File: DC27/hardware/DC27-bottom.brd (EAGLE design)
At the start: 102.4 x 117.6 mm, 95 parts, among them IC2 LDL112D33R, IC3 FT2232HL-REEL, IC4 93LC46BT-I_OT, J1 PAIRING, J2 JTAG, J3 Battery, J4 Program Port, U2 ESP-WROOM-32, Y1 ABM7-12.000MHZ-D2Y-T

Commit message: moved vias
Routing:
- net PROG_TX: track 63.8 -> 66.4 mm
- net PAIR_RX: track 133.3 -> 134.6 mm
- net PAIR_TX: track 132.0 -> 131.4 mm

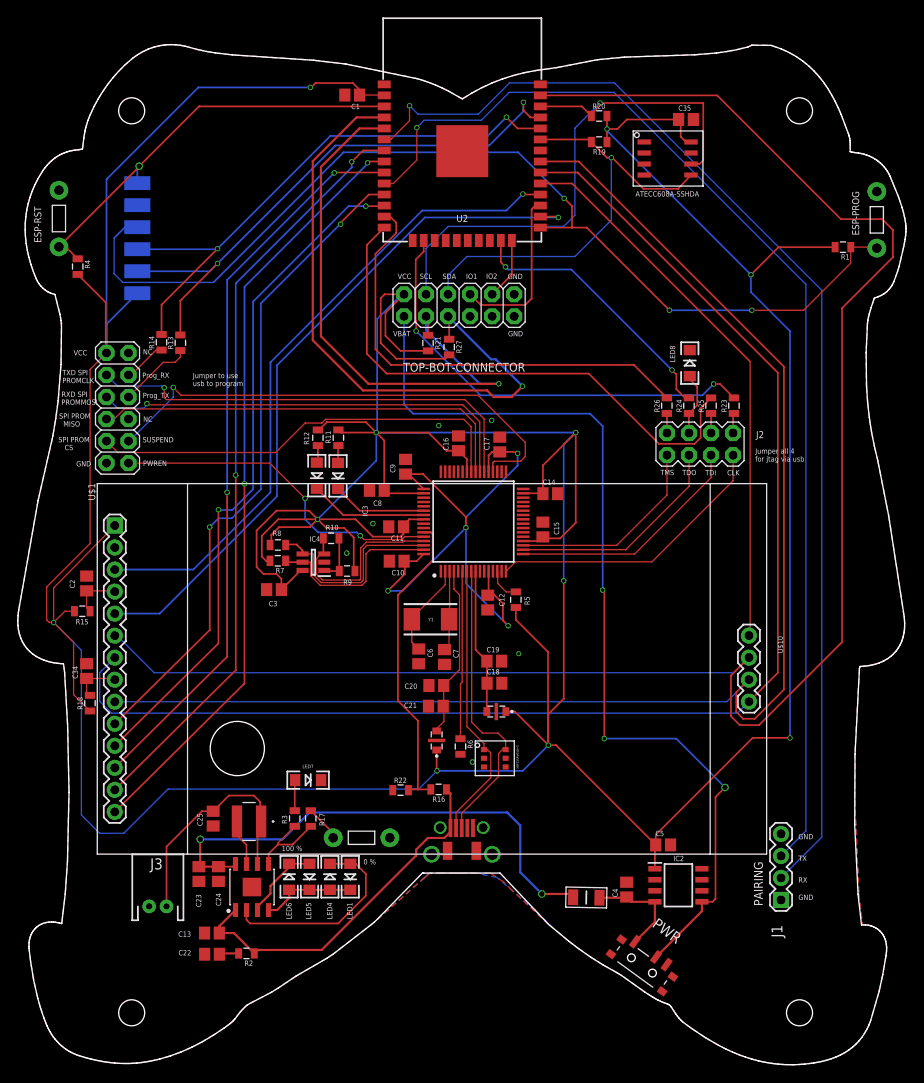
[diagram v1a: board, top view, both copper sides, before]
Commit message: Fixed the darknet logo, and made resistors pretty
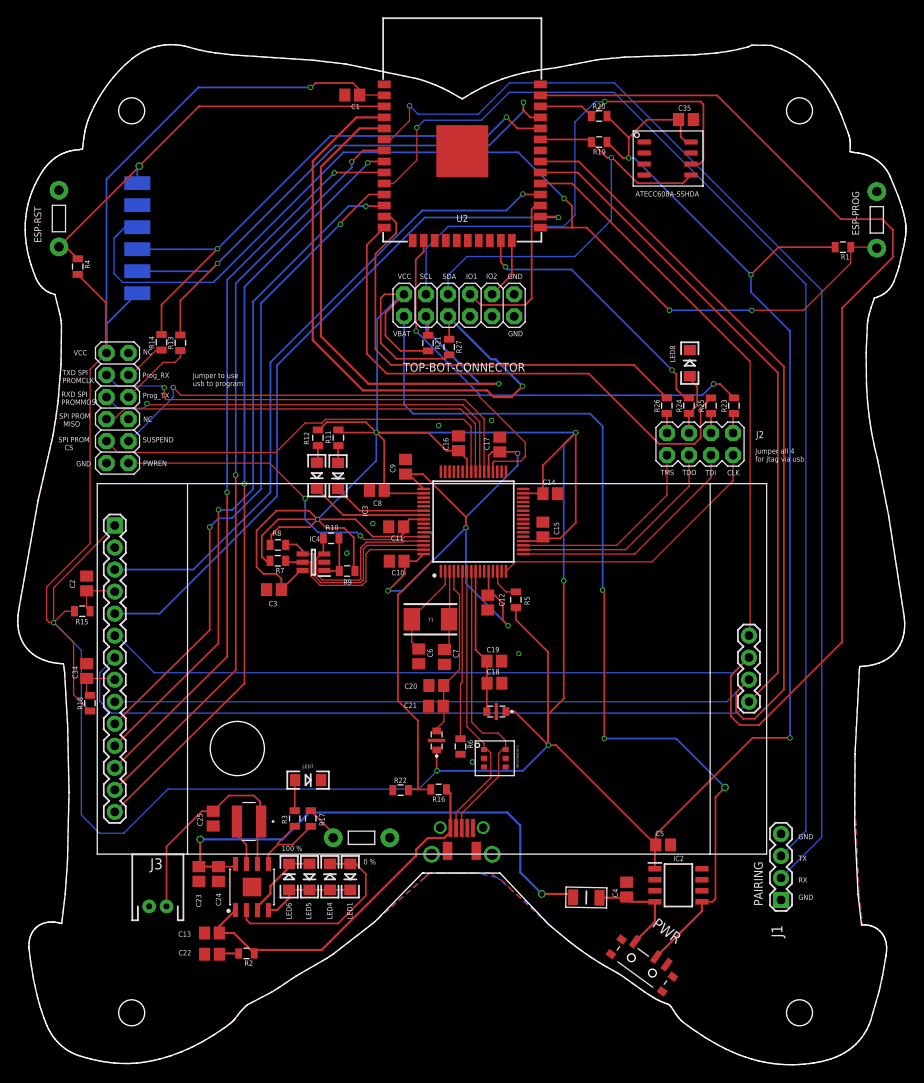
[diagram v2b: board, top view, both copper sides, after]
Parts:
- U$9: value DN_LOGO -> DN_LOGODC26; device logos:DN_LOGO_LONG_SILK -> darknet_parts_library:DN_LOGO_DC26
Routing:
- net SCL: track 66.4 -> 67.4 mm
- net SDA: track 51.3 -> 50.7 mm

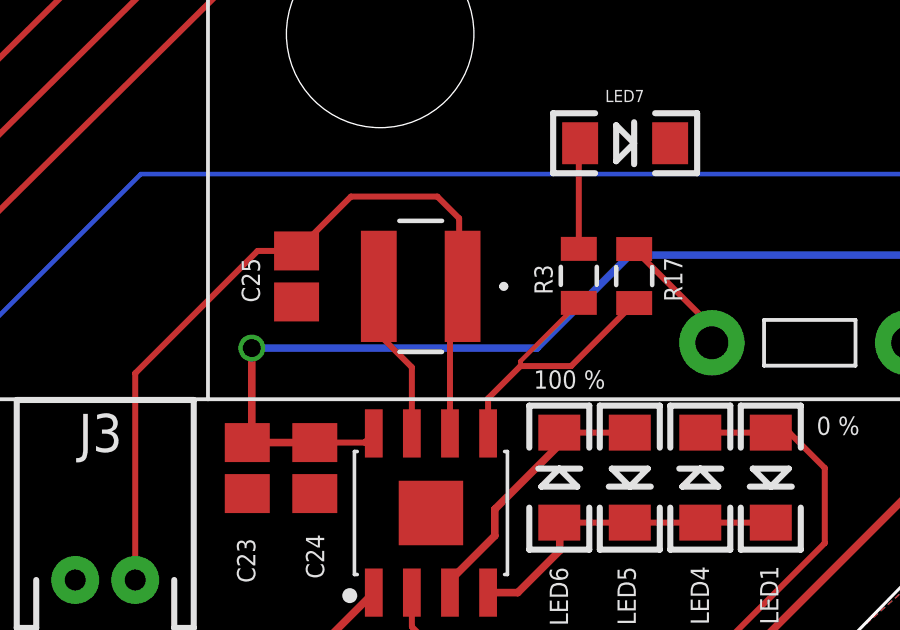
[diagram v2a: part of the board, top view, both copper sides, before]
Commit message: fixed an airwire, changed diodes to through hole
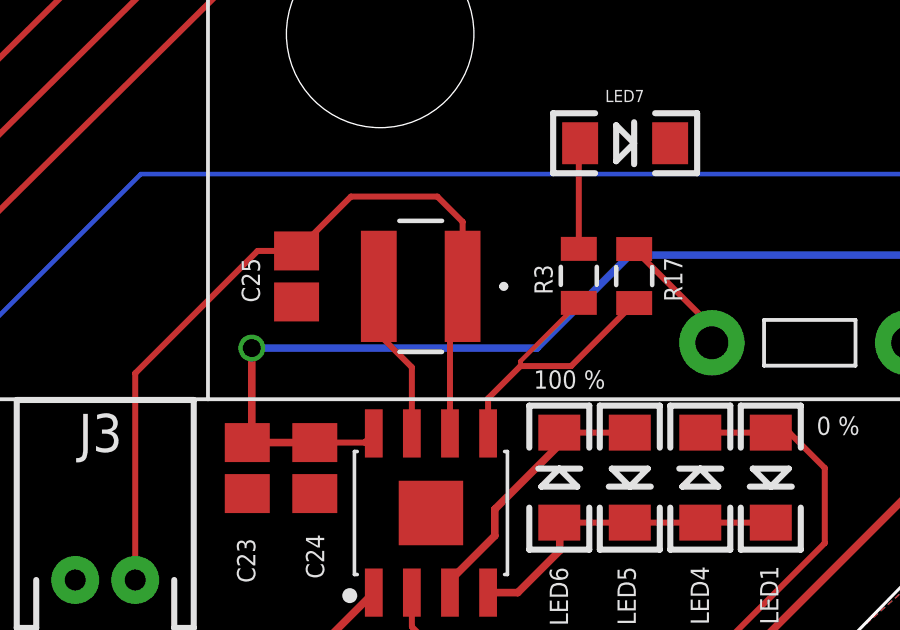
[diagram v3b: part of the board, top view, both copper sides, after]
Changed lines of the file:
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@@
 <?xml version="1.0" encoding="utf-8"?>
 <!DOCTYPE eagle SYSTEM "eagle.dtd">
-<eagle version="9.4.0">
+<eagle version="9.4.1">
 <drawing>
 <settings>
-<setting alwaysvectorfont="no"/>
+<setting alwaysvectorfont="yes"/>
 <setting keepoldvectorfont="yes"/>
 <setting verticaltext="up"/>
@@
 <layer number="14" name="Route14" color="22" fill="1" visible="no" active="no"/>
 <layer number="15" name="Route15" color="23" fill="1" visible="no" active="no"/>
-<layer number="16" name="Bottom" color="1" fill="1" visible="no" active="yes"/>
+<layer number="16" name="Bottom" color="1" fill="1" visible="yes" active="yes"/>
 <layer number="17" name="Pads" color="2" fill="1" visible="yes" active="yes"/>
 <layer number="18" name="Vias" color="2" fill="1" visible="yes" active="yes"/>
@@
 <layer number="20" name="Dimension" color="24" fill="1" visible="yes" active="yes"/>
 <layer number="21" name="tPlace" color="7" fill="1" visible="yes" active="yes"/>
-<layer number="22" name="bPlace" color="7" fill="1" visible="no" active="yes"/>
+<layer number="22" name="bPlace" color="7" fill="1" visible="yes" active="yes"/>
 <layer number="23" name="tOrigins" color="15" fill="1" visible="yes" active="yes"/>
-<layer number="24" name="bOrigins" color="15" fill="1" visible="no" active="yes"/>
+<layer number="24" name="bOrigins" color="15" fill="1" visible="yes" active="yes"/>
 <layer number="25" name="tNames" color="7" fill="1" visible="yes" active="yes"/>
-<layer number="26" name="bNames" color="7" fill="1" visible="no" active="yes"/>
+<layer number="26" name="bNames" color="7" fill="1" visible="yes" active="yes"/>
 <layer number="27" name="tValues" color="7" fill="1" visible="no" active="yes"/>
 <layer number="28" name="bValues" color="7" fill="1" visible="no" active="yes"/>
@@
 <layer number="38" name="bTest" color="7" fill="1" visible="no" active="yes"/>
 <layer number="39" name="tKeepout" color="4" fill="11" visible="yes" active="yes"/>
-<layer number="40" name="bKeepout" color="1" fill="11" visible="no" active="yes"/>
+<layer number="40" name="bKeepout" color="1" fill="11" visible="yes" active="yes"/>
 <layer number="41" name="tRestrict" color="4" fill="10" visible="yes" active="yes"/>
-<layer number="42" name="bRestrict" color="1" fill="10" visible="no" active="yes"/>
+<layer number="42" name="bRestrict" color="1" fill="10" visible="yes" active="yes"/>
 <layer number="43" name="vRestrict" color="2" fill="10" visible="no" active="yes"/>
 <layer number="44" name="Drills" color="7" fill="1" visible="no" active="yes"/>
-<layer number="45" name="Holes" color="7" fill="1" visible="yes" active="yes"/>
+<layer number="45" name="Holes" color="7" fill="1" visible="no" active="yes"/>
 <layer number="46" name="Milling" color="3" fill="1" visible="no" active="yes"/>
 <layer number="47" name="Measures" color="7" fill="1" visible="no" active="yes"/>
@@
 <layer number="50" name="dxf" color="7" fill="1" visible="no" active="no"/>
 <layer number="51" name="tDocu" color="7" fill="1" visible="yes" active="yes"/>
-<layer number="52" name="bDocu" color="7" fill="1" visible="no" active="yes"/>
+<layer number="52" name="bDocu" color="7" fill="1" visible="yes" active="yes"/>
 <layer number="53" name="tGND_GNDA" color="7" fill="9" visible="no" active="no"/>
 <layer number="54" name="bGND_GNDA" color="1" fill="9" visible="no" active="no"/>
@@
 <contactref element="C25" pad="1"/>
 <contactref element="J3" pad="2"/>
-<wire x1="28.061628125" y1="28.045459375" x2="28.061628125" y2="28.2" width="0.2" layer="1"/>
 <wire x1="22.526540625" y1="29.226628125" x2="21.226628125" y2="29.226628125" width="0.2" layer="1"/>
 <wire x1="17.149028125" y1="25.149028125" x2="17.149028125" y2="18.258659375" width="0.2" layer="1"/>
 <wire x1="21.226628125" y1="29.226628125" x2="17.149028125" y2="25.149028125" width="0.2" layer="1"/>
-<wire x1="27.640428125" y1="27.7788" x2="28.061628125" y2="28.2" width="0.2" layer="1"/>
-<wire x1="27.640428125" y1="23.144359375" x2="27.640428125" y2="27.7788" width="0.2" layer="1"/>
 <wire x1="24.33815625" y1="31.03824375" x2="27.22058125" y2="31.03824375" width="0.2" layer="1"/>
 <wire x1="24.33815625" y1="31.03824375" x2="22.526540625" y2="29.226628125" width="0.2" layer="1"/>
-<wire x1="27.22058125" y1="31.03824375" x2="27.9457375" y2="30.3130875" width="0.2" layer="1"/>
-<wire x1="27.9457375" y1="30.3130875" x2="27.9457375" y2="28.7218875" width="0.2" layer="1"/>
-<wire x1="27.9457375" y1="28.7218875" x2="28.061628125" y2="28.2" width="0" layer="19" extent="1-1"/>
+<wire x1="27.640428125" y1="23.144359375" x2="27.640428125" y2="27.624259375" width="0.2" layer="1"/>
+<wire x1="27.640428125" y1="27.624259375" x2="28.061628125" y2="28.045459375" width="0.2" layer="1"/>
+<wire x1="27.22058125" y1="31.03824375" x2="28.061628125" y2="30.197196875" width="0.2" layer="1"/>
+<wire x1="28.061628125" y1="30.197196875" x2="28.061628125" y2="28.045459375" width="0.2" layer="1"/>
 </signal>
 <signal name="N$21">

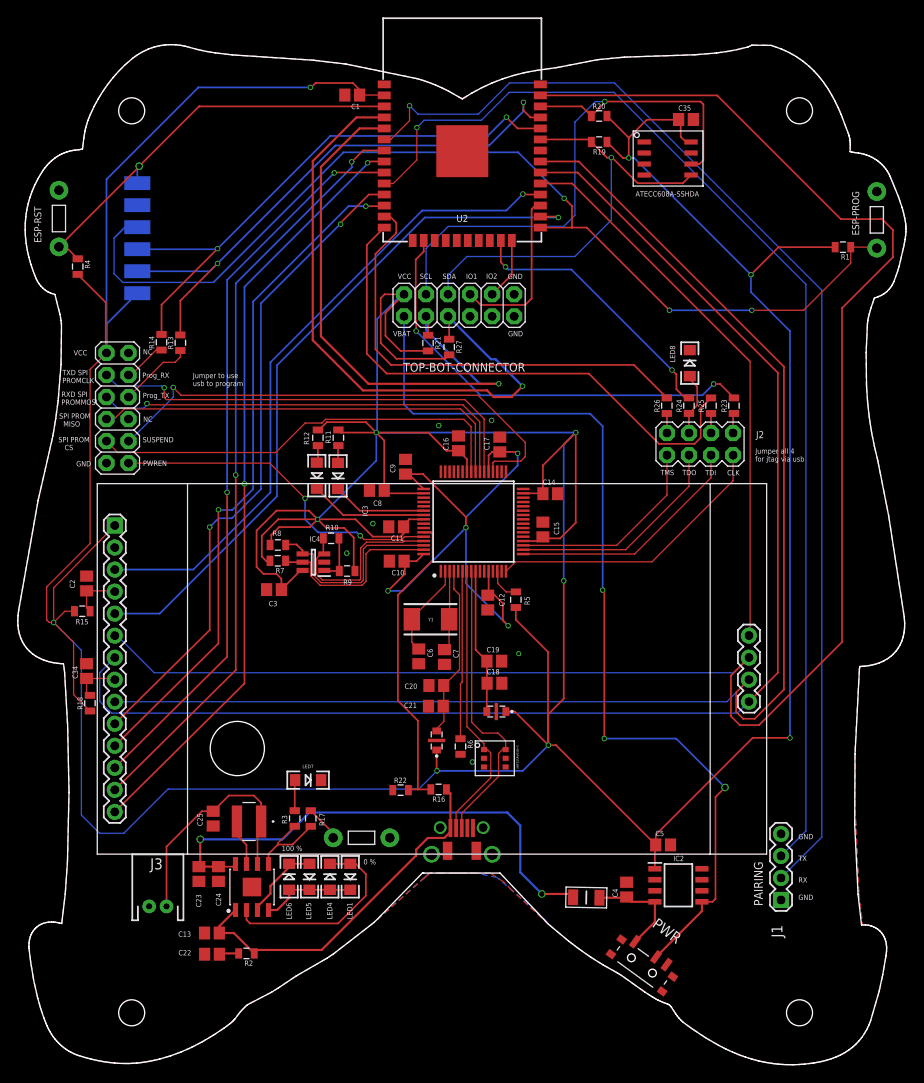
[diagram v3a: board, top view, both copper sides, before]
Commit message: final tweaks moved top board I2C to separate bus
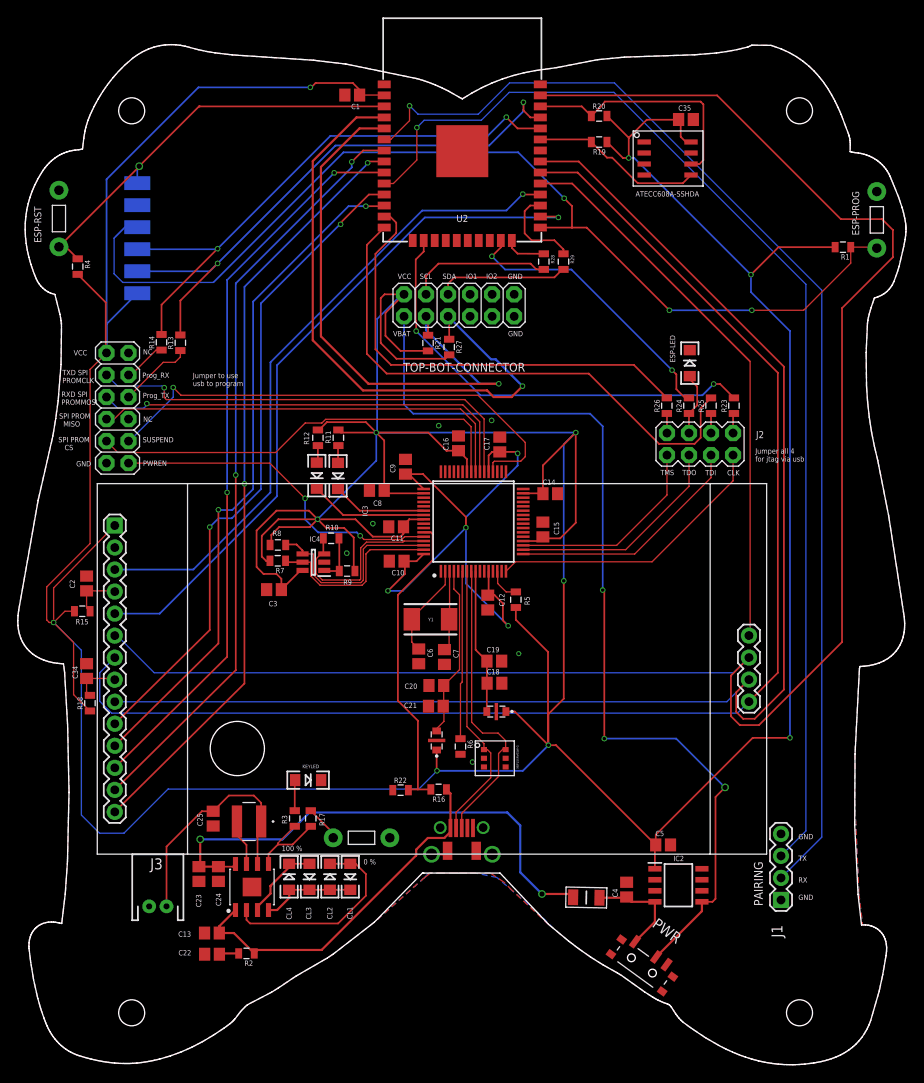
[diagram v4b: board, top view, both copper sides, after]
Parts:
- added R28, R29: 2.2 K, dc-26:0805
- CL1: value cl1 -> BLUE
- CL2: value cl2 -> BLUE
- CL3: value cl3 -> BLUE
- CL4: value cl4 -> BLUE
- ESP-LED: value ESP-LED -> GREEN
- KEYLED: value KeyLed -> GREEN
- R19, R20: value 4.7 K -> 2.2 K
- RX-LED: value rx-led -> BLUE
- TX-LED: value tx-led -> GREEN
- renumbered LED1 to CL1, LED2 to RX-LED, LED3 to TX-LED, LED4 to CL2, LED5 to CL3, LED6 to CL4, LED7 to KEYLED, LED8 to ESP-LED
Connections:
- removed net APA102_CLK: TOP-BOT-CONNECTOR.10, U2.24
- removed net APA102_DATA: TOP-BOT-CONNECTOR.8, U2.27
- new net N$1: R28.2, TOP-BOT-CONNECTOR.4
- new net N$2: R29.2, TOP-BOT-CONNECTOR.6
- new net SCL-2: R28.1, U2.24
- new net SDA-2: R29.1, U2.27
- net SCL: no longer TOP-BOT-CONNECTOR.4
- net SDA: no longer TOP-BOT-CONNECTOR.6
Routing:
- net SCL: track 67.4 -> 28.2 mm, vias 1 -> 0
- net SDA: track 50.7 -> 19.9 mm, vias 1 -> 0
- net APA102_DATA: track 19.4 -> 0.00 mm
- net N$1: track 0.00 -> 16.5 mm
- net N$2: track 0.00 -> 15.2 mm
- net SDA-2: track 0.00 -> 10.4 mm
- net APA102_CLK: track 7.15 -> 0.00 mm
- net SCL-2: track 0.00 -> 4.81 mm
- net JTAG_TDO_LED1: track 31.7 -> 32.7 mm
